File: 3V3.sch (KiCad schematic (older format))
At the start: 0 parts

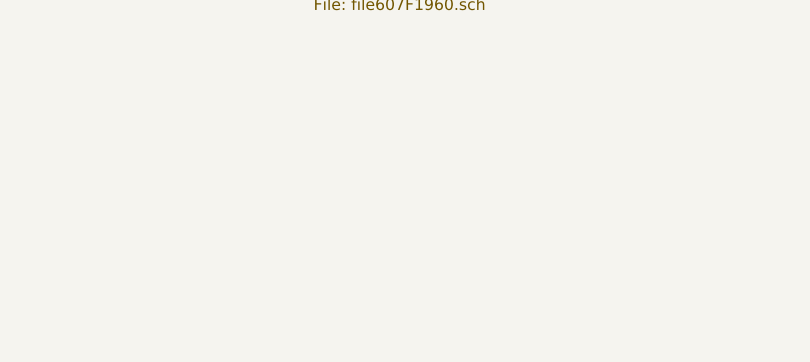
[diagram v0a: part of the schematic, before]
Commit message: added data logging
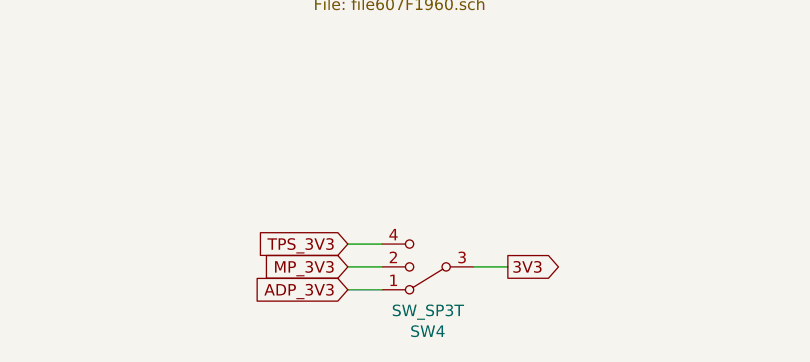
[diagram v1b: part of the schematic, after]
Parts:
- added SW4: SW_SP3T, symbol Switch:SW_SP3T
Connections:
- new net 3V3: SW4.3
- new net ADP_3V3: SW4.1
- new net MP_3V3: SW4.2
- new net TPS_3V3: SW4.4
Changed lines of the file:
@@
 $Descr A4 11693 8268
 encoding utf-8
-Sheet 2 5
+Sheet 2 10
 Title ""
 Date ""
@@
 F1 "file6086062F.sch" 50
 $EndSheet
+Text GLabel 3650 3450 0    50   Input ~ 0
+TPS_3V3
+Wire Wire Line
+	3650 3450 3800 3450
+Text GLabel 3650 3550 0    50   Input ~ 0
+MP_3V3
+Text GLabel 3650 3650 0    50   Input ~ 0
+ADP_3V3
+Wire Wire Line
+	3800 3650 3650 3650
+Wire Wire Line
+	4200 3550 4350 3550
+Text GLabel 4350 3550 2    50   Output ~ 0
+3V3
+$Comp
+L Switch:SW_SP3T SW4
+U 1 1 608026A5
+P 4000 3550
+F 0 "SW4" H 4000 3833 50  0000 C CNN
+F 1 "SW_SP3T" H 4000 3742 50  0000 C CNN
+F 2 "" H 3375 3725 50  0001 C CNN
+F 3 "~" H 3375 3725 50  0001 C CNN
+	1    4000 3550
+	-1   0    0    1
+$EndComp
+Wire Wire Line
+	3650 3550 3800 3550
 $EndSCHEMATC

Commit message: full schematic, version 1.0
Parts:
- removed SW4: SW_SP3T, symbol Switch:SW_SP3T
- added D10, D8, D9: LED_Small, Diode_SMD:D_0603_1608Metric_Pad1.05x0.95mm_HandSolder, symbol Device:LED_Small
- added R38, R39, R40: 500R, Resistor_SMD:R_0805_2012Metric_Pad1.20x1.40mm_HandSolder, symbol Device:R_Small
- added S11: OS103012MU1QP1, EIPP:SW_OS103012MU1QP1, symbol EIPP_LIBRARY:OS103012MU1QP1
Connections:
- net 3V3: now also S11.1
- net ADP_3V3: now also R40.1, S11.4
- net MP_3V3: now also R39.1, S11.3
- net TPS_3V3: now also R38.1, S11.2
- new net: D8.2 (A), R38.2
- new net: D9.2 (A), R39.2
- new net: D10.2 (A), R40.2
- new net GND: D10.1 (K), D8.1 (K), D9.1 (K)
- no-connect marks 0 -> 2
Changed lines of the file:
@@
 $Descr A4 11693 8268
 encoding utf-8
-Sheet 2 10
+Sheet 2 15
 Title ""
 Date ""
@@
 F1 "file6086062F.sch" 50
 $EndSheet
-Text GLabel 3650 3450 0    50   Input ~ 0
+Text GLabel 2050 4200 0    50   Input ~ 0
 TPS_3V3
-Wire Wire Line
-	3650 3450 3800 3450
-Text GLabel 3650 3550 0    50   Input ~ 0
+Text GLabel 2050 4300 0    50   Input ~ 0
 MP_3V3
-Text GLabel 3650 3650 0    50   Input ~ 0
+Text GLabel 2050 4400 0    50   Input ~ 0
 ADP_3V3
 Wire Wire Line
-	3800 3650 3650 3650
-Wire Wire Line
-	4200 3550 4350 3550
-Text GLabel 4350 3550 2    50   Output ~ 0
+	3250 4000 3100 4000
+Text GLabel 3100 4000 0    50   Output ~ 0
 3V3
 $Comp
-L Switch:SW_SP3T SW4
-U 1 1 608026A5
-P 4000 3550
-F 0 "SW4" H 4000 3833 50  0000 C CNN
-F 1 "SW_SP3T" H 4000 3742 50  0000 C CNN
-F 2 "" H 3375 3725 50  0001 C CNN
-F 3 "~" H 3375 3725 50  0001 C CNN
-	1    4000 3550
-	-1   0    0    1
-$EndComp
-Wire Wire Line
-	3650 3550 3800 3550
+L EIPP_LIBRARY:OS103012MU1QP1 S11
+U 1 1 608F895B
+P 3650 4300
+F 0 "S11" H 3880 4346 50  0000 L CNN
+F 1 "OS103012MU1QP1" H 3880 4255 50  0000 L CNN
+F 2 "EIPP:SW_OS103012MU1QP1" H 3650 4300 50  0001 L BNN
+F 3 "" H 3650 4300 50  0001 L BNN
+F 4 "9.2 mm" H 3650 4300 50  0001 L BNN "MAXIMUM_PACKAGE_HEIGHT"
+F 5 "C and K Switches" H 3650 4300 50  0001 L BNN "MANUFACTURER"
+F 6 "Manufacturer Recommendations" H 3650 4300 50  0001 L BNN "STANDARD"
+F 7 "8 Aug 17" H 3650 4300 50  0001 L BNN "PARTREV"
+	1    3650 4300
+	1    0    0    -1
+$EndComp
+Wire Wire Line
+	3250 4550 3150 4550
+Wire Wire Line
+	3150 4600 3250 4600
+NoConn ~ 3150 4550
+NoConn ~ 3150 4600
+$Comp
+L Device:LED_Small D?
+U 1 1 6082CA23
+P 2350 5050
+AR Path="/60925CA4/6082CA23" Ref="D?"  Part="1"
+AR Path="/607D64D2/6082CA23" Ref="D8"  Part="1"
+F 0 "D8" V 2396 4980 50  0000 R CNN
+F 1 "LED_Small" V 2305 4980 50  0000 R CNN
+F 2 "Diode_SMD:D_0603_1608Metric_Pad1.05x0.95mm_HandSolder" V 2350 5050 50  0001 C CNN
+F 3 "~" V 2350 5050 50  0001 C CNN
+	1    2350 5050
+	0    -1   -1   0
+$EndComp
+$Comp
+L Device:R_Small R?
+U 1 1 6082CA29
+P 2350 4800
+AR Path="/60925CA4/6082CA29" Ref="R?"  Part="1"
+AR Path="/607D64D2/6082CA29" Ref="R38"  Part="1"
+F 0 "R38" H 2409 4846 50  0000 L CNN
+F 1 "500R" H 2409 4755 50  0000 L CNN
+F 2 "Resistor_SMD:R_0805_2012Metric_Pad1.20x1.40mm_HandSolder" H 2350 4800 50  0001 C CNN
+F 3 "~" H 2350 4800 50  0001 C CNN
+	1    2350 4800
+	1    0    0    -1
+$EndComp
+Wire Wire Line
+	2350 4950 2350 4900
+Wire Wire Line
+	2350 4700 2350 4200
+Wire Wire Line
+	2350 5150 2350 5350
+$Comp
+L power:GND #PWR?
+U 1 1 6082CA32
+P 2350 5350
+AR Path="/60925CA4/6082CA32" Ref="#PWR?"  Part="1"
+AR Path="/607D64D2/6082CA32" Ref="#PWR059"  Part="1"
+F 0 "#PWR059" H 2350 5100 50  0001 C CNN
+F 1 "GND" H 2355 5177 50  0000 C CNN
+F 2 "" H 2350 5350 50  0001 C CNN
+F 3 "" H 2350 5350 50  0001 C CNN
+	1    2350 5350
+	1    0    0    -1
+$EndComp
+$Comp
+L Device:LED_Small D?
+U 1 1 6082CA38
+P 2650 5050
+AR Path="/60925CA4/6082CA38" Ref="D?"  Part="1"
+AR Path="/607D64D2/6082CA38" Ref="D9"  Part="1"
+F 0 "D9" V 2696 4980 50  0000 R CNN
+F 1 "LED_Small" V 2605 4980 50  0000 R CNN
+F 2 "Diode_SMD:D_0603_1608Metric_Pad1.05x0.95mm_HandSolder" V 2650 5050 50  0001 C CNN
+F 3 "~" V 2650 5050 50  0001 C CNN
+	1    2650 5050
+	0    -1   -1   0
+$EndComp
+$Comp
+L Device:R_Small R?
+U 1 1 6082CA3E
+P 2650 4800
+AR Path="/60925CA4/6082CA3E" Ref="R?"  Part="1"
+AR Path="/607D64D2/6082CA3E" Ref="R39"  Part="1"
+F 0 "R39" H 2709 4846 50  0000 L CNN
+F 1 "500R" H 2709 4755 50  0000 L CNN
+F 2 "Resistor_SMD:R_0805_2012Metric_Pad1.20x1.40mm_HandSolder" H 2650 4800 50  0001 C CNN
+F 3 "~" H 2650 4800 50  0001 C CNN
+	1    2650 4800
+	1    0    0    -1
+$EndComp
+Wire Wire Line
+	2650 4950 2650 4900
+Wire Wire Line
+	2650 5150 2650 5350
+$Comp
+L power:GND #PWR?
+U 1 1 6082CA46
+P 2650 5350
+AR Path="/60925CA4/6082CA46" Ref="#PWR?"  Part="1"
+AR Path="/607D64D2/6082CA46" Ref="#PWR060"  Part="1"
+F 0 "#PWR060" H 2650 5100 50  0001 C CNN
+F 1 "GND" H 2655 5177 50  0000 C CNN
+F 2 "" H 2650 5350 50  0001 C CNN
+F 3 "" H 2650 5350 50  0001 C CNN
+	1    2650 5350
+	1    0    0    -1
+$EndComp
+$Comp
+L Device:LED_Small D?
+U 1 1 6082CA4C
+P 2950 5050
+AR Path="/60925CA4/6082CA4C" Ref="D?"  Part="1"
+AR Path="/607D64D2/6082CA4C" Ref="D10"  Part="1"
+F 0 "D10" V 2996 4980 50  0000 R CNN
+F 1 "LED_Small" V 2905 4980 50  0000 R CNN
+F 2 "Diode_SMD:D_0603_1608Metric_Pad1.05x0.95mm_HandSolder" V 2950 5050 50  0001 C CNN
+F 3 "~" V 2950 5050 50  0001 C CNN
+	1    2950 5050
+	0    -1   -1   0
+$EndComp
+$Comp
+L Device:R_Small R?
+U 1 1 6082CA52
+P 2950 4800
+AR Path="/60925CA4/6082CA52" Ref="R?"  Part="1"
+AR Path="/607D64D2/6082CA52" Ref="R40"  Part="1"
+F 0 "R40" H 3009 4846 50  0000 L CNN
+F 1 "500R" H 3009 4755 50  0000 L CNN
+F 2 "Resistor_SMD:R_0805_2012Metric_Pad1.20x1.40mm_HandSolder" H 2950 4800 50  0001 C CNN
+F 3 "~" H 2950 4800 50  0001 C CNN
+	1    2950 4800
+	1    0    0    -1
+$EndComp
+Wire Wire Line
+	2950 4950 2950 4900
+Wire Wire Line
+	2950 5150 2950 5350
+$Comp
+L power:GND #PWR?
+U 1 1 6082CA5A
+P 2950 5350
+AR Path="/60925CA4/6082CA5A" Ref="#PWR?"  Part="1"
+AR Path="/607D64D2/6082CA5A" Ref="#PWR061"  Part="1"
+F 0 "#PWR061" H 2950 5100 50  0001 C CNN
+F 1 "GND" H 2955 5177 50  0000 C CNN
+F 2 "" H 2950 5350 50  0001 C CNN
+F 3 "" H 2950 5350 50  0001 C CNN
+	1    2950 5350
+	1    0    0    -1
+$EndComp
+Wire Wire Line
+	2650 4300 2650 4700
+Wire Wire Line
+	2950 4400 2950 4700
+Wire Wire Line
+	2950 4400 3250 4400
+Wire Wire Line
+	2950 4400 2050 4400
+Connection ~ 2950 4400
+Wire Wire Line
+	2050 4300 2650 4300
+Wire Wire Line
+	2650 4300 3250 4300
+Connection ~ 2650 4300
+Wire Wire Line
+	2350 4200 3250 4200
+Wire Wire Line
+	2350 4200 2050 4200
+Connection ~ 2350 4200
 $EndSCHEMATC
